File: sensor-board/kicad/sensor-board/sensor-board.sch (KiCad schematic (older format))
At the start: 13 parts, among them J1 Conn_01x04_Female, J2 Conn_01x02_Female, J3 Conn_01x03_Female, J4 Conn_01x02_Female, U1 LM324, U2 ATtiny25-20SU

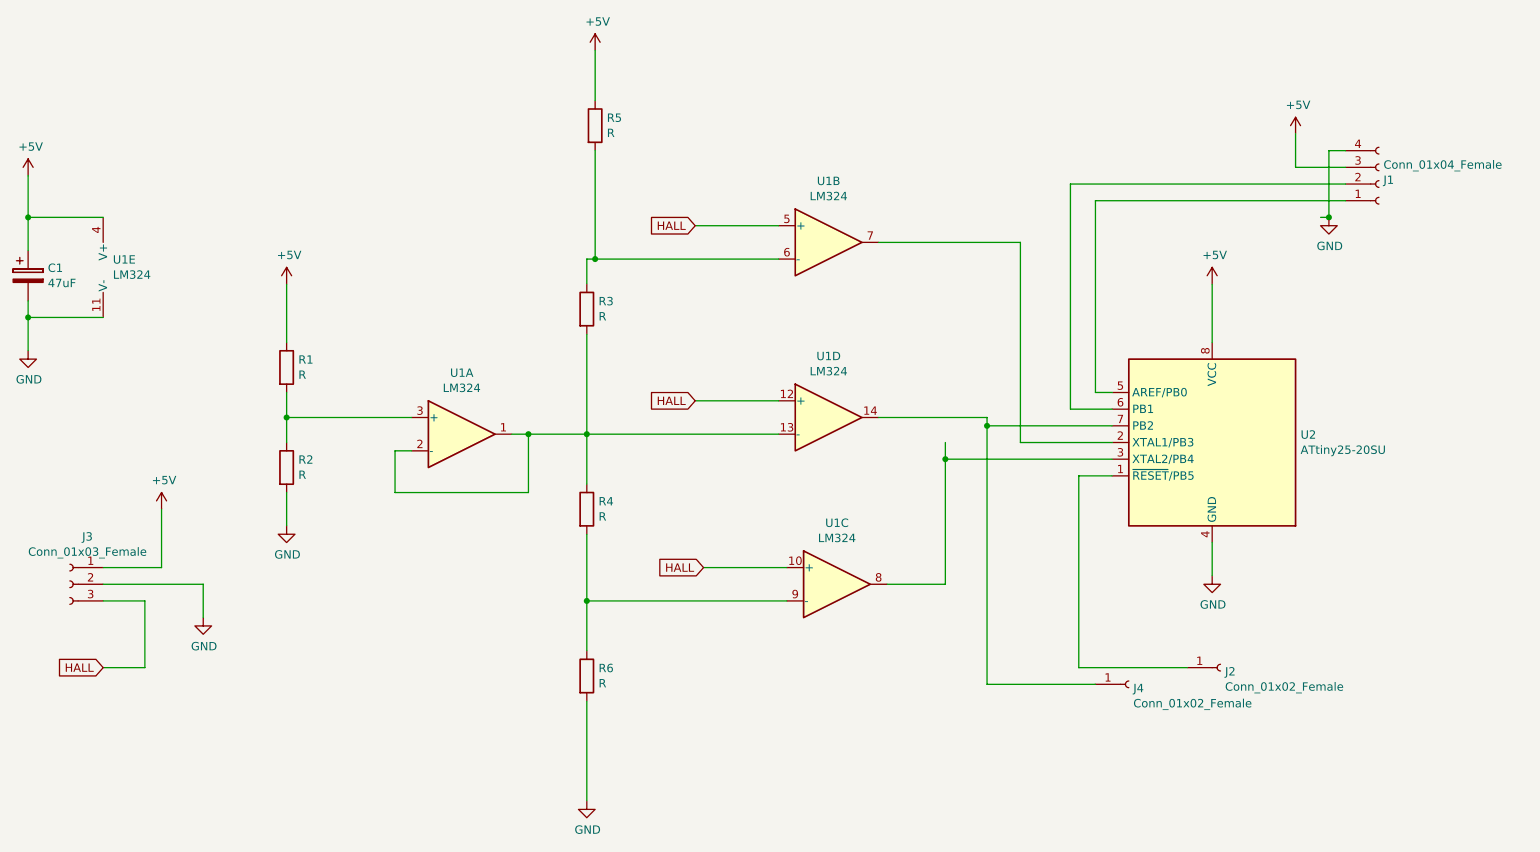
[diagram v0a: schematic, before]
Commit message: Sensor-board: revize 2
Opravená chyba: Operační zesilovač má silnější výstup než programátor,
takže kompletně sestavená revize 1 nelze snadno flashnout.
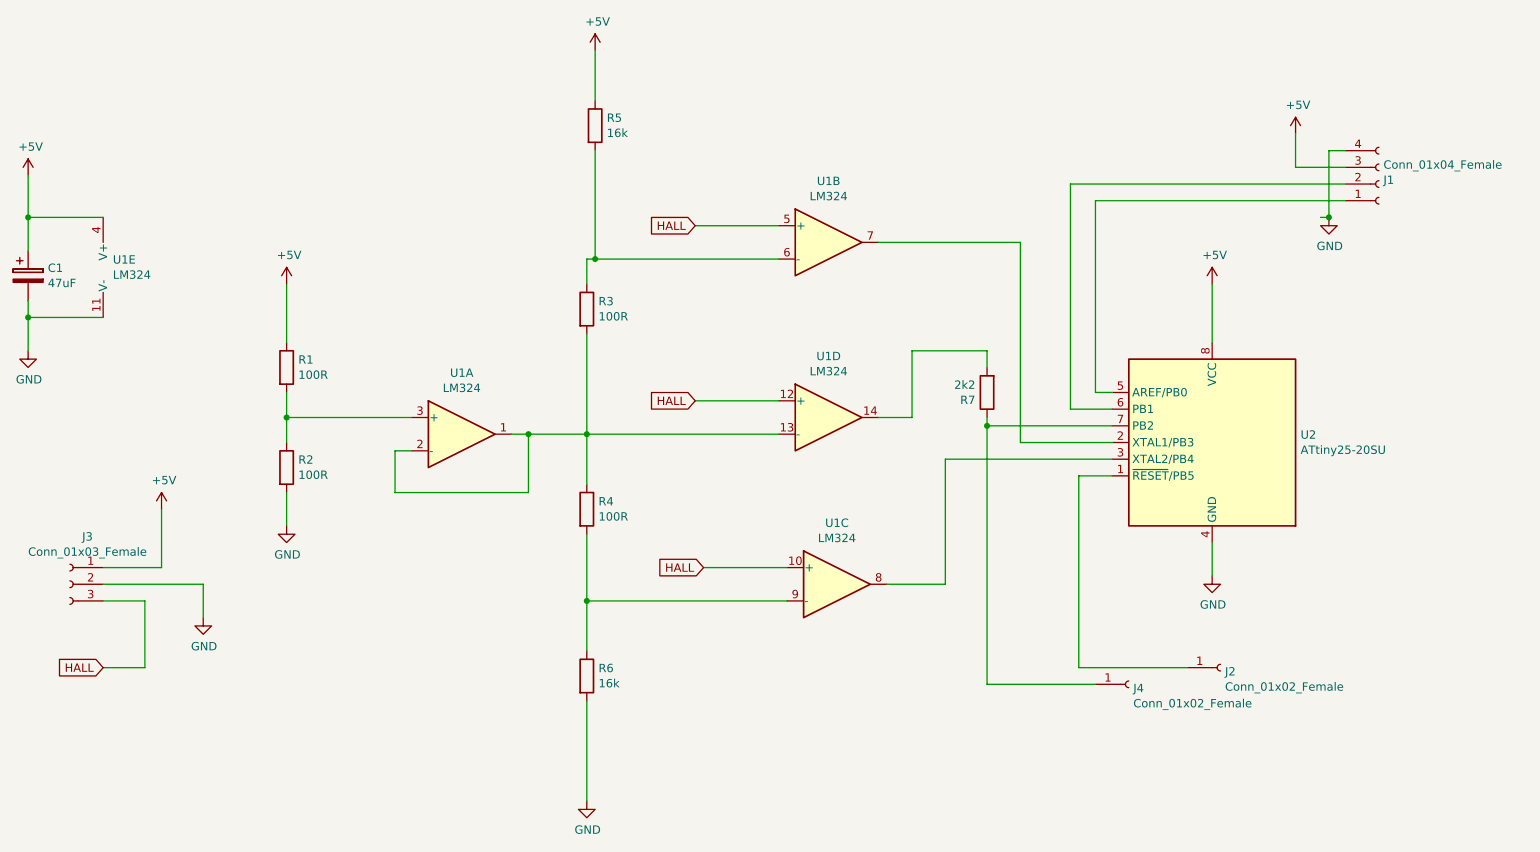
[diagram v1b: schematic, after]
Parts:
- added R7: 2k2, Resistor_SMD:R_1206_3216Metric_Pad1.42x1.75mm_HandSolder, symbol Device:R
- R1, R2, R3, R4: value R -> 100R
- R5, R6: value R -> 16k
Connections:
- wire segments 67 -> 69
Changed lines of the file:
@@
 P 2750 3000
 F 0 "R1" H 2820 3046 50  0000 L CNN
-F 1 "R" H 2820 2955 50  0000 L CNN
+F 1 "100R" H 2820 2955 50  0000 L CNN
 F 2 "Resistor_SMD:R_1206_3216Metric_Pad1.42x1.75mm_HandSolder" V 2680 3000 50  0001 C CNN
 F 3 "~" H 2750 3000 50  0001 C CNN
@@
 P 2750 3600
 F 0 "R2" H 2820 3646 50  0000 L CNN
-F 1 "R" H 2820 3555 50  0000 L CNN
+F 1 "100R" H 2820 3555 50  0000 L CNN
 F 2 "Resistor_SMD:R_1206_3216Metric_Pad1.42x1.75mm_HandSolder" V 2680 3600 50  0001 C CNN
 F 3 "~" H 2750 3600 50  0001 C CNN
@@
 P 4550 2650
 F 0 "R3" H 4620 2696 50  0000 L CNN
-F 1 "R" H 4620 2605 50  0000 L CNN
+F 1 "100R" H 4620 2605 50  0000 L CNN
 F 2 "Resistor_SMD:R_1206_3216Metric_Pad1.42x1.75mm_HandSolder" V 4480 2650 50  0001 C CNN
 F 3 "~" H 4550 2650 50  0001 C CNN
@@
 P 4550 3850
 F 0 "R4" H 4620 3896 50  0000 L CNN
-F 1 "R" H 4620 3805 50  0000 L CNN
+F 1 "100R" H 4620 3805 50  0000 L CNN
 F 2 "Resistor_SMD:R_1206_3216Metric_Pad1.42x1.75mm_HandSolder" V 4480 3850 50  0001 C CNN
 F 3 "~" H 4550 3850 50  0001 C CNN
@@
 	6950 3350 6950 3300
 Wire Wire Line
-	6950 3300 6300 3300
-Wire Wire Line
 	6700 4300 6350 4300
 Wire Wire Line
@@
 	1900 4400 1900 4800
 Wire Wire Line
-	6700 3450 6700 3550
-Wire Wire Line
 	9100 1900 7450 1900
 Wire Wire Line
@@
 P 4550 4850
 F 0 "R6" H 4620 4896 50  0000 L CNN
-F 1 "R" H 4620 4805 50  0000 L CNN
+F 1 "16k" H 4620 4805 50  0000 L CNN
 F 2 "Resistor_SMD:R_1206_3216Metric_Pad1.42x1.75mm_HandSolder" V 4480 4850 50  0001 C CNN
 F 3 "~" H 4550 4850 50  0001 C CNN
@@
 P 4600 1550
 F 0 "R5" H 4670 1596 50  0000 L CNN
-F 1 "R" H 4670 1505 50  0000 L CNN
+F 1 "16k" H 4670 1505 50  0000 L CNN
 F 2 "Resistor_SMD:R_1206_3216Metric_Pad1.42x1.75mm_HandSolder" V 4530 1550 50  0001 C CNN
 F 3 "~" H 4600 1550 50  0001 C CNN
@@
 Wire Wire Line
 	7700 3550 6700 3550
-Connection ~ 6700 3550
 Wire Wire Line
 	6700 3550 6700 4300
@@
 	9000 2100 8950 2100
 Connection ~ 9000 2100
+$Comp
+L Device:R R7
+U 1 1 5C6DC7CA
+P 6950 3150
+F 0 "R7" H 7020 3196 50  0000 L CNN
+F 1 "2k2" H 7020 3105 50  0000 L CNN
+F 2 "Resistor_SMD:R_1206_3216Metric_Pad1.42x1.75mm_HandSolder" V 6880 3150 50  0001 C CNN
+F 3 "~" H 6950 3150 50  0001 C CNN
+	1    6950 3150
+	-1   0    0    1
+$EndComp
+Wire Wire Line
+	6500 3300 6300 3300
+Wire Wire Line
+	6950 3000 6950 2900
+Wire Wire Line
+	6950 2900 6500 2900
+Wire Wire Line
+	6500 2900 6500 3300
 $EndSCHEMATC
